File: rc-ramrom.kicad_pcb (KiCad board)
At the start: 2 copper layers, 99.1 x 49.9 mm, 24 parts, among them J1 RC2014, U1 EPROM, U2 AS6C1008, U3 74HCT4075, U4 74HCT74, U5 74HCT138

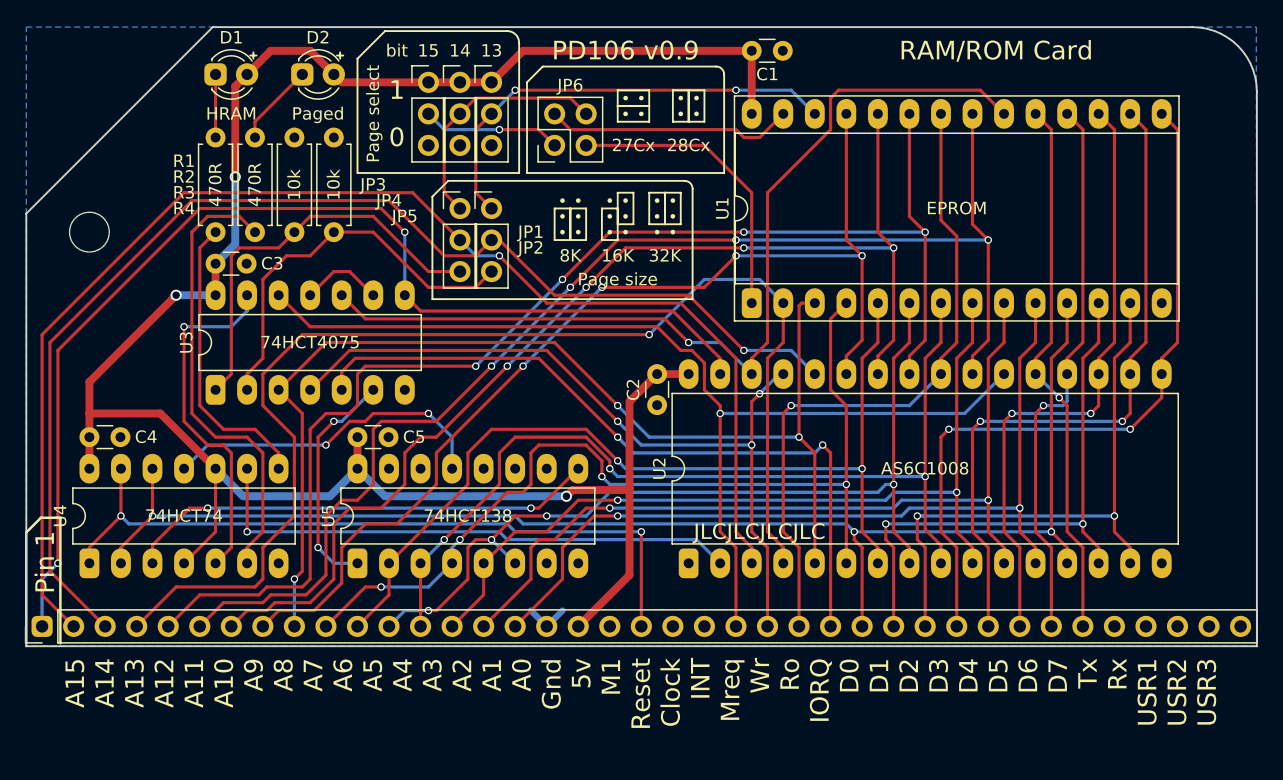
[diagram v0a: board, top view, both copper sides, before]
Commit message: Neatened routing
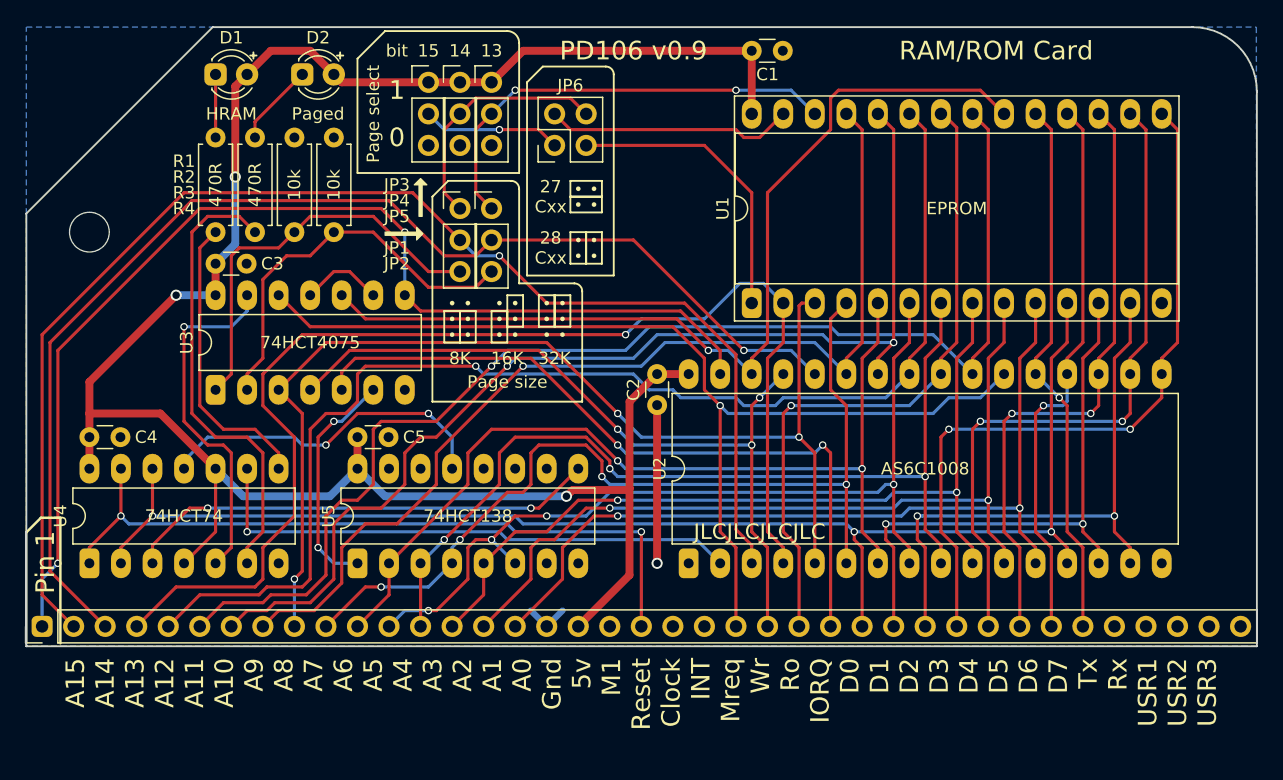
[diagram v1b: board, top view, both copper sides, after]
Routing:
- net GND: track 3.59 -> 16.3 mm, vias 0 -> 1
- net A11: track 104.7 -> 101.1 mm, vias 4 -> 1
- net A8: track 85.8 -> 82.7 mm, vias 4 -> 1
- net A9: track 92.1 -> 89.4 mm, vias 4 -> 2
- net A10: track 103.8 -> 101.2 mm, vias 4 -> 1
- net /~HRAM_CFG: track 26.8 -> 27.7 mm
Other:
- board text added: "27 Cxx"
- board text added: "28 Cxx"
- board text added: "For 27C512, set jumpers as above Set bit 15 high for 27C256 & 28C256 Set bits 15 and 14 high for 27C128 As above, and remove bit 13 for 27C64 Set 15 high, remove 13 & 14 for 28C64"
- board text added: "Notes for page select jumpers: 8K page size uses all select jumpers For 16K page size, remove bit 13 For 32K page size, remove bits 13 & 14"
- board text removed: "27Cx"
- board text removed: "28Cx"
- board text removed: "8K page size uses all select jumpers For 16K page size, remove JP5 For 32K page size, remove JP4 & JP5"
- board text removed: "For 27C512, set jumpers as above Set JP3 high for 27C256 & 28C256 Set JP3 and JP4 high for 27C128 As above, and remove JP5 for 27C64"

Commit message: Updated silk, moved to v1.0
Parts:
- D1: value Yellow -> Green
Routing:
- net +5V: track 172.5 -> 169.1 mm
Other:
- rule pad_to_mask_clearance: 0.127 -> 0
- board text added: "27C512: Set jumpers as above 27C256 & 28C256: Set bit 15 high 27C128: Set bits 15 and 14 high 27C64: As above, and remove bit 13 28C64: Set 15 high, remove 13 & 14"
- board text added: "Notes for page select jumpers: 8K page size uses all select jumpers For 16K pages, remove bit 13 For 32K pages, remove bits 13 & 14"
- board text added: "PD106 v1.0"
- board text added: "RAM/ROM Card PD106 v1.0"
- board text removed: "For 27C512, set jumpers as above Set bit 15 high for 27C256 & 28C256 Set bits 15 and 14 high for 27C128 As above, and remove bit 13 for 27C64 Set 15 high, remove 13 & 14 for 28C64"
- board text removed: "Notes for page select jumpers: 8K page size uses all select jumpers For 16K page size, remove bit 13 For 32K page size, remove bits 13 & 14"
- board text removed: "PD106 v0.9"
- board text removed: "RAM/ROM Card PD106 v0.9"
